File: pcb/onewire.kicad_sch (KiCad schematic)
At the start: 7 parts, among them J15 Conn_01x03, J16 Conn_01x03, J17 Screw_Terminal_01x03, Q1 BSS138, U1 DS18B20

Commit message: Use larger screw terminals, adjust layout to suit
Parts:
- removed J17: Screw_Terminal_01x03, Conn_ScrewTerminals:ED5553DS, symbol Connector:Screw_Terminal_01x03
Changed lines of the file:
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@@
 	(label "ONEWIRE_5V"
 		(at 173.99 114.3 0)
-		(fields_autoplaced yes)
 		(effects
 			(font
@@
 	)
 	(label "ONEWIRE_5V"
-		(at 76.2 160.02 0)
-		(fields_autoplaced yes)
+		(at 114.3 63.5 0)
 		(effects
 			(font
@@
 	)
 	(label "ONEWIRE_5V"
-		(at 114.3 63.5 0)
-		(fields_autoplaced yes)
+		(at 76.2 109.22 0)
 		(effects
 			(font
@@
 	)
 	(label "ONEWIRE_5V"
-		(at 76.2 109.22 0)
-		(fields_autoplaced yes)
+		(at 76.2 134.62 0)
 		(effects
 			(font
@@
 		)
 	)
-	(label "ONEWIRE_5V"
-		(at 76.2 134.62 0)
-		(fields_autoplaced yes)
+	(hierarchical_label "OneWire"
+		(shape bidirectional)
+		(at 63.5 63.5 180)
 		(effects
 			(font
 				(size 1.27 1.27)
 			)
-			(justify left bottom)
-		)
-	)
-	(hierarchical_label "OneWire"
-		(shape bidirectional)
-		(at 63.5 63.5 180)
-		(fields_autoplaced yes)
-		(effects
-			(font
-				(size 1.27 1.27)
-			)
 			(justify right)
 		)
@@
 	)
 	(symbol
-		(lib_id "power:+5V")
-		(at 76.2 162.56 270)
-		(unit 1)
-		(exclude_from_sim no)
-		(in_bom yes)
-		(on_board yes)
-		(dnp no)
-		(fields_autoplaced yes)
-		(property "Reference" "#PWR039"
-			(at 72.39 162.56 0)
-			(effects
-				(font
-					(size 1.27 1.27)
-				)
-				(hide yes)
-			)
-		)
-		(property "Value" "+5V"
-			(at 80.01 162.5599 90)
-			(effects
-				(font
-					(size 1.27 1.27)
-				)
-				(justify left)
-			)
-		)
-		(property "Footprint" ""
-			(at 76.2 162.56 0)
-			(effects
-				(font
-					(size 1.27 1.27)
-				)
-				(hide yes)
-			)
-		)
-		(property "Datasheet" ""
-			(at 76.2 162.56 0)
-			(effects
-				(font
-					(size 1.27 1.27)
-				)
-				(hide yes)
-			)
-		)
-		(property "Description" "Power symbol creates a global label with name \"+5V\""
-			(at 76.2 162.56 0)
-			(effects
-				(font
-					(size 1.27 1.27)
-				)
-				(hide yes)
-			)
-		)
-		(pin "1"
-		)
-		(instances
-			(project "pico-plc"
-				(path "/fc9ff52a-d720-4efe-8661-3db6c88a54e4/41233123-d0bb-4504-988d-344ca09ddc46"
-					(reference "#PWR039")
-					(unit 1)
-				)
-			)
-		)
-	)
-	(symbol
 		(lib_id "power:+3V3")
 		(at 76.2 44.45 0)
@@
 	)
 	(symbol
-		(lib_id "Connector:Screw_Terminal_01x03")
-		(at 71.12 162.56 180)
-		(unit 1)
-		(exclude_from_sim no)
-		(in_bom yes)
-		(on_board yes)
-		(dnp no)
-		(fields_autoplaced yes)
-		(property "Reference" "J17"
-			(at 71.12 153.67 0)
-			(effects
-				(font
-					(size 1.27 1.27)
-				)
-			)
-		)
-		(property "Value" "Screw_Terminal_01x03"
-			(at 71.12 156.21 0)
-			(effects
-				(font
-					(size 1.27 1.27)
-				)
-			)
-		)
-		(property "Footprint" "Conn_ScrewTerminals:ED5553DS"
-			(at 71.12 162.56 0)
-			(effects
-				(font
-					(size 1.27 1.27)
-				)
-				(hide yes)
-			)
-		)
-		(property "Datasheet" "~"
-			(at 71.12 162.56 0)
-			(effects
-				(font
-					(size 1.27 1.27)
-				)
-				(hide yes)
-			)
-		)
-		(property "Description" "Generic screw terminal, single row, 01x03, script generated (kicad-library-utils/schlib/autogen/connector/)"
-			(at 71.12 162.56 0)
-			(effects
-				(font
-					(size 1.27 1.27)
-				)
-				(hide yes)
-			)
-		)
-		(pin "3"
-		)
-		(pin "2"
-		)
-		(pin "1"
-		)
-		(instances
-			(project ""
-				(path "/fc9ff52a-d720-4efe-8661-3db6c88a54e4/41233123-d0bb-4504-988d-344ca09ddc46"
-					(reference "J17")
-					(unit 1)
-				)
-			)
-		)
-	)
-	(symbol
 		(lib_id "power:+5V")
 		(at 76.2 137.16 270)
@@
 					(unit 1)
 				)
-			)
-		)
-	)
-	(symbol
-		(lib_id "power:GND")
-		(at 76.2 165.1 90)
-		(unit 1)
-		(exclude_from_sim no)
-		(in_bom yes)
-		(on_board yes)
-		(dnp no)
-		(fields_autoplaced yes)
-		(property "Reference" "#PWR040"
-			(at 82.55 165.1 0)
-			(effects
-				(font
-					(size 1.27 1.27)
-				)
-				(hide yes)
-			)
-		)
-		(property "Value" "GND"
-			(at 80.01 165.0999 90)
-			(effects
-				(font
-					(size 1.27 1.27)
-				)
-				(justify right)
-			)
-		)
-		(property "Footprint" ""
-			(at 76.2 165.1 0)
-			(effects
-				(font
-					(size 1.27 1.27)
-				)
-				(hide yes)
-			)
-		)
-		(property "Datasheet" ""
-			(at 76.2 165.1 0)
-			(effects
-				(font
-					(size 1.27 1.27)
-				)
-				(hide yes)
-			)
-		)
-		(property "Description" "Power symbol creates a global label with name \"GND\" , ground"
-			(at 76.2 165.1 0)
-			(effects
-				(font
-					(size 1.27 1.27)
-				)
-				(hide yes)
-			)
-		)
-		(pin "1"
-		)
-		(instances
-			(project "pico-plc"
-				(path "/fc9ff52a-d720-4efe-8661-3db6c88a54e4/41233123-d0bb-4504-988d-344ca09ddc46"
-					(reference "#PWR040")
-					(unit 1)
-				)

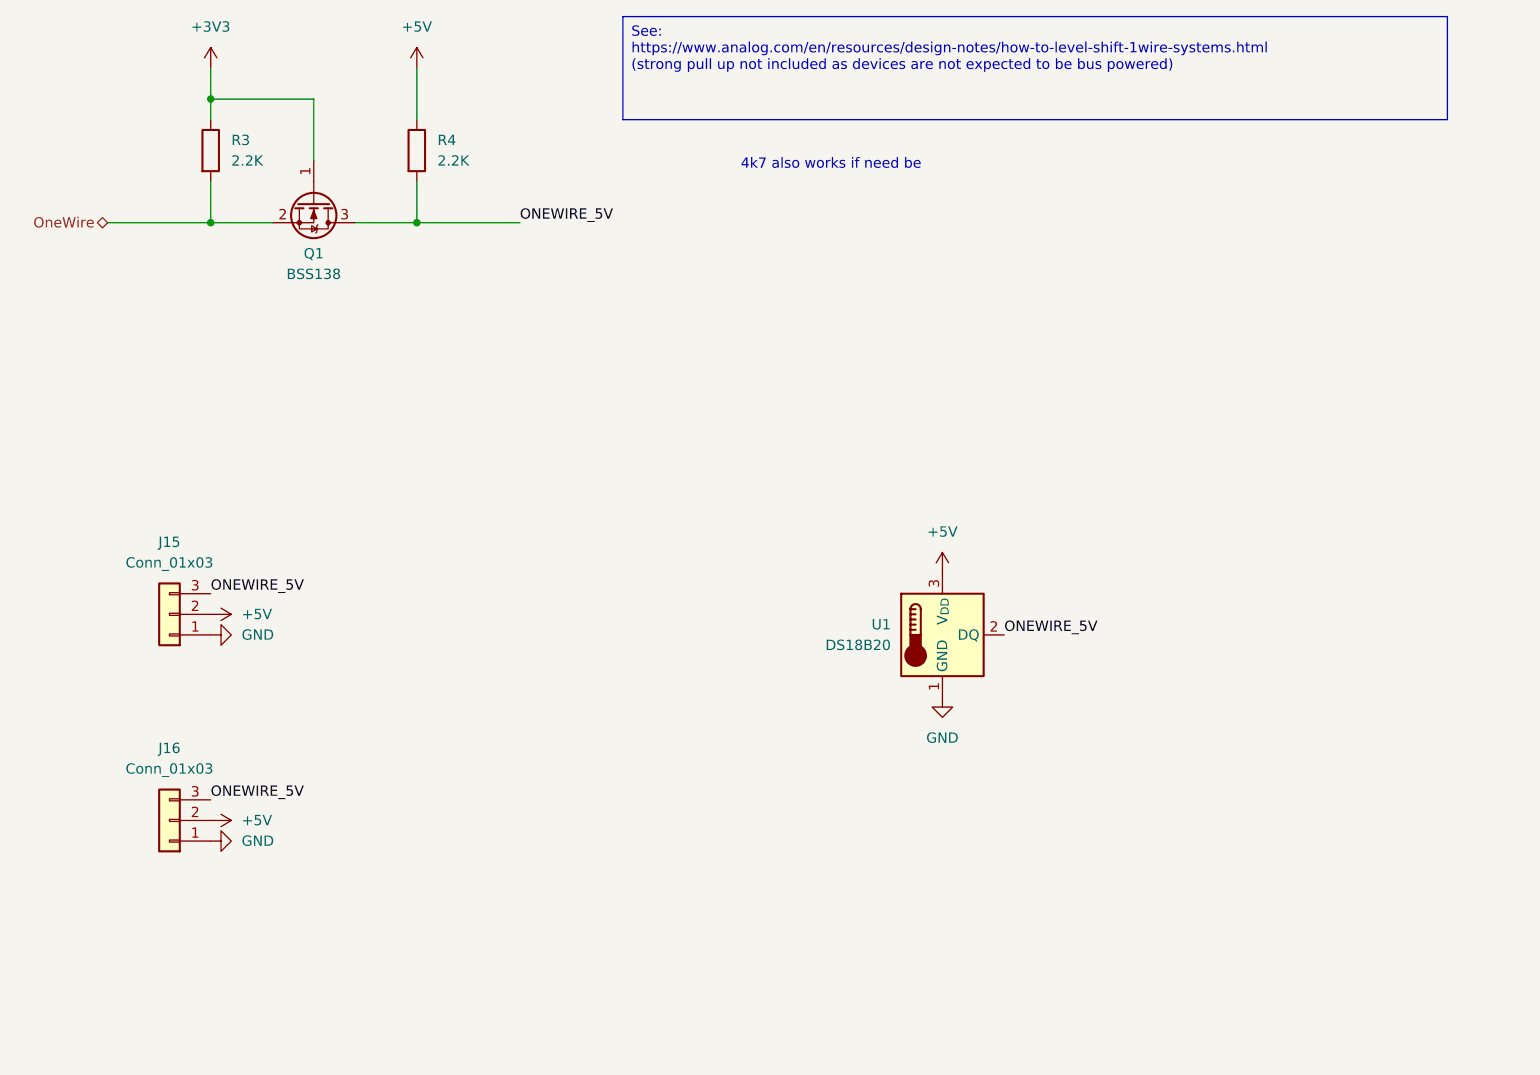
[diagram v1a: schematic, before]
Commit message: Convert PCB to KiCad 9 project
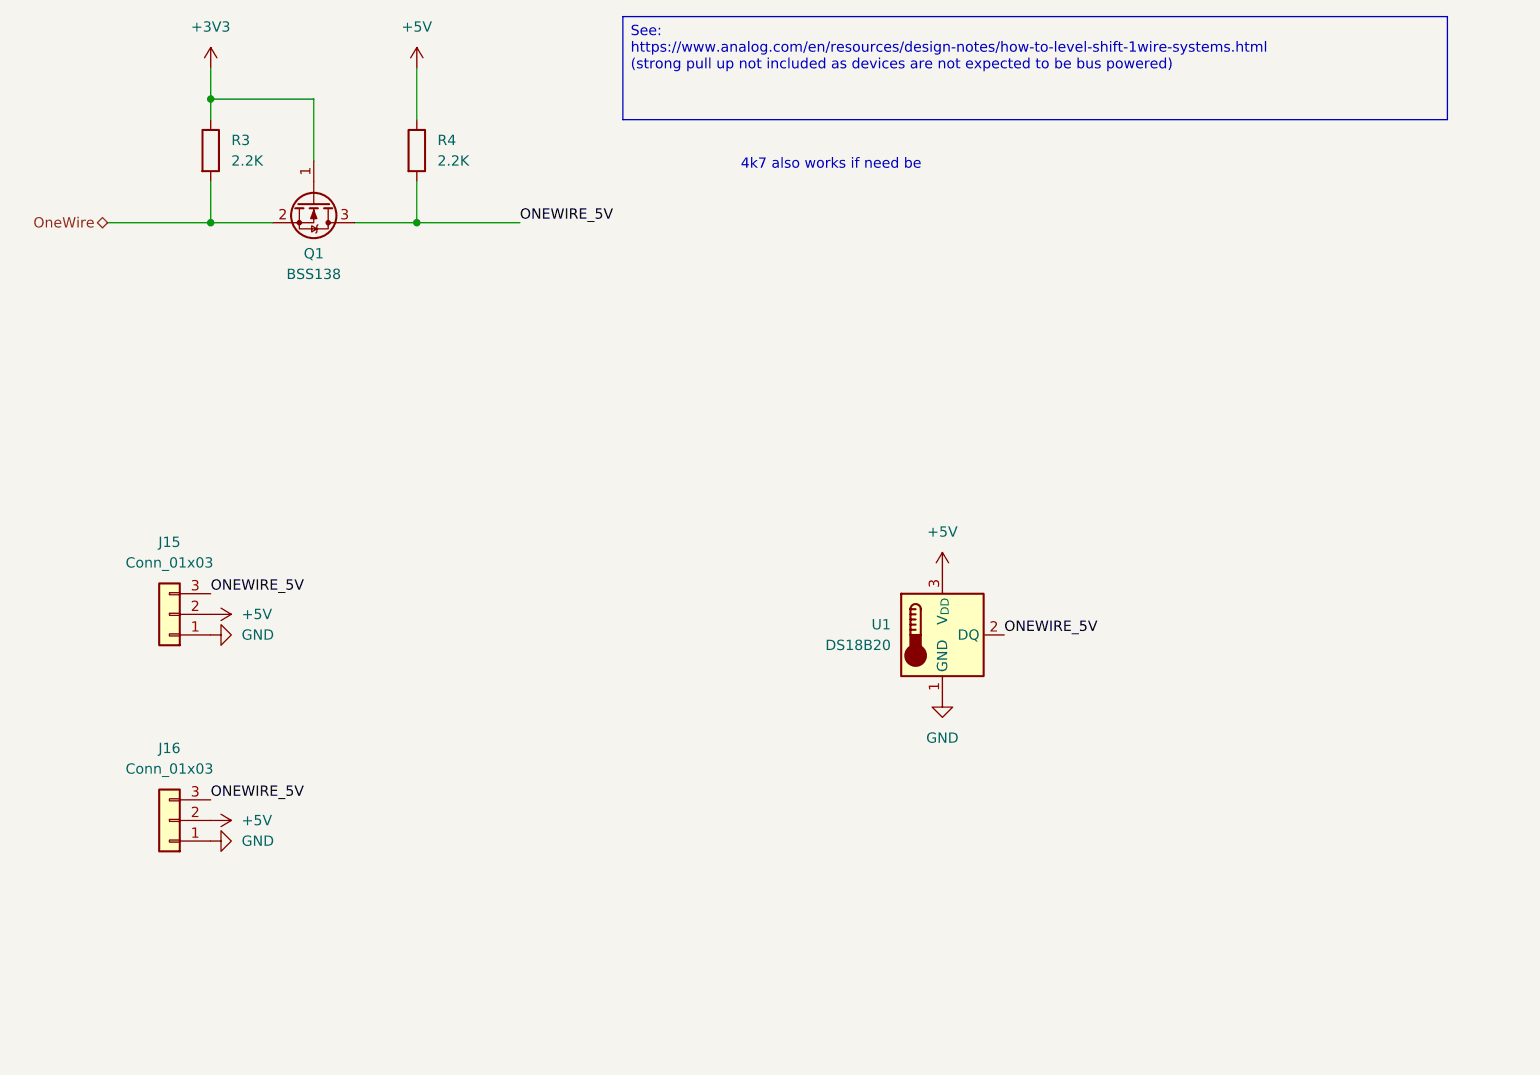
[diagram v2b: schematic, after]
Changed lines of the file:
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@@
 (kicad_sch
-	(version 20231120)
+	(version 20250114)
 	(generator "eeschema")
-	(generator_version "8.0")
+	(generator_version "9.0")
 	(paper "A4")
+	(text "4k7 also works if need be"
+		(exclude_from_sim no)
+		(at 152.654 56.388 0)
+		(effects
+			(font
+				(size 1.27 1.27)
+			)
+		)
+	)
+	(text_box "See:\nhttps://www.analog.com/en/resources/design-notes/how-to-level-shift-1wire-systems.html\n(strong pull up not included as devices are not expected to be bus powered)"
+		(exclude_from_sim no)
+		(at 127 38.1 0)
+		(size 101.6 12.7)
+		(margins 0.9525 0.9525 0.9525 0.9525)
+		(stroke
+			(width 0)
+			(type default)
+		)
+		(fill
+			(type none)
+		)
+		(effects
+			(font
+				(size 1.27 1.27)
+			)
+			(justify left top)
+		)
+	)
 	(junction
 		(at 101.6 63.5)
@@
 		)
 	)
-	(text_box "See:\nhttps://www.analog.com/en/resources/design-notes/how-to-level-shift-1wire-systems.html\n(strong pull up not included as devices are not expected to be bus powered)"
-		(exclude_from_sim no)
-		(at 127 38.1 0)
-		(size 101.6 12.7)
-		(stroke
-			(width 0)
-			(type default)
-		)
-		(fill
-			(type none)
-		)
-		(effects
-			(font
-				(size 1.27 1.27)
-			)
-			(justify left top)
-		)
-	)
-	(text "4k7 also works if need be"
-		(exclude_from_sim no)
-		(at 152.654 56.388 0)
-		(effects
-			(font
-				(size 1.27 1.27)
-			)
-		)
-	)
